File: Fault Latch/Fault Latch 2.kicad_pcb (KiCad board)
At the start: 2 copper layers, 85 x 85 mm, 116 parts, among them J1 1053141312, J3 1053131202, J4 1053131202, J5 1053131202, K3 Fujitsu_FTR-LYCA005x, K5 Fujitsu_FTR-LYCA005x, K6 Fujitsu_FTR-LYCA005x, Q101 Q_NPN_BEC, Q102 Q_NPN_BEC, Q103 Q_NPN_BEC, Q104 Q_NPN_BEC, Q105 Q_NMOS_GSD, Q106 Q_NMOS_GSD, Q110 Q_NPN_BEC, Q111 Q_NPN_BEC, Q112 Q_NMOS_GSD, Q113 Q_NMOS_GSD, Q114 Q_NMOS_GSD, Q115 Q_NMOS_GSD, Q117 Q_NMOS_GSD, Q118 Q_NMOS_GSD, Q119 Q_NMOS_GSD, Q120 Q_NMOS_GSD, Q121 Q_NMOS_GSD, Q122 Q_NMOS_GSD, Q123 Q_NMOS_GSD, Q124 Q_NMOS_GSD, Q125 Q_NMOS_GSD, SW101 SW_Omron_B3FS, SW102 SW_Omron_B3FS, SW103 SW_Omron_B3FS, U1 74LS279, U104 74AHC1G00, U109 74AHC1G00, U112 74AHC1G00, U117 74AHC1G00, U118 LM555xM, U2 LM1117DT-5.0, U7 SN74AHC1G08DBVR, U8 SN74AHC1G08DBVR

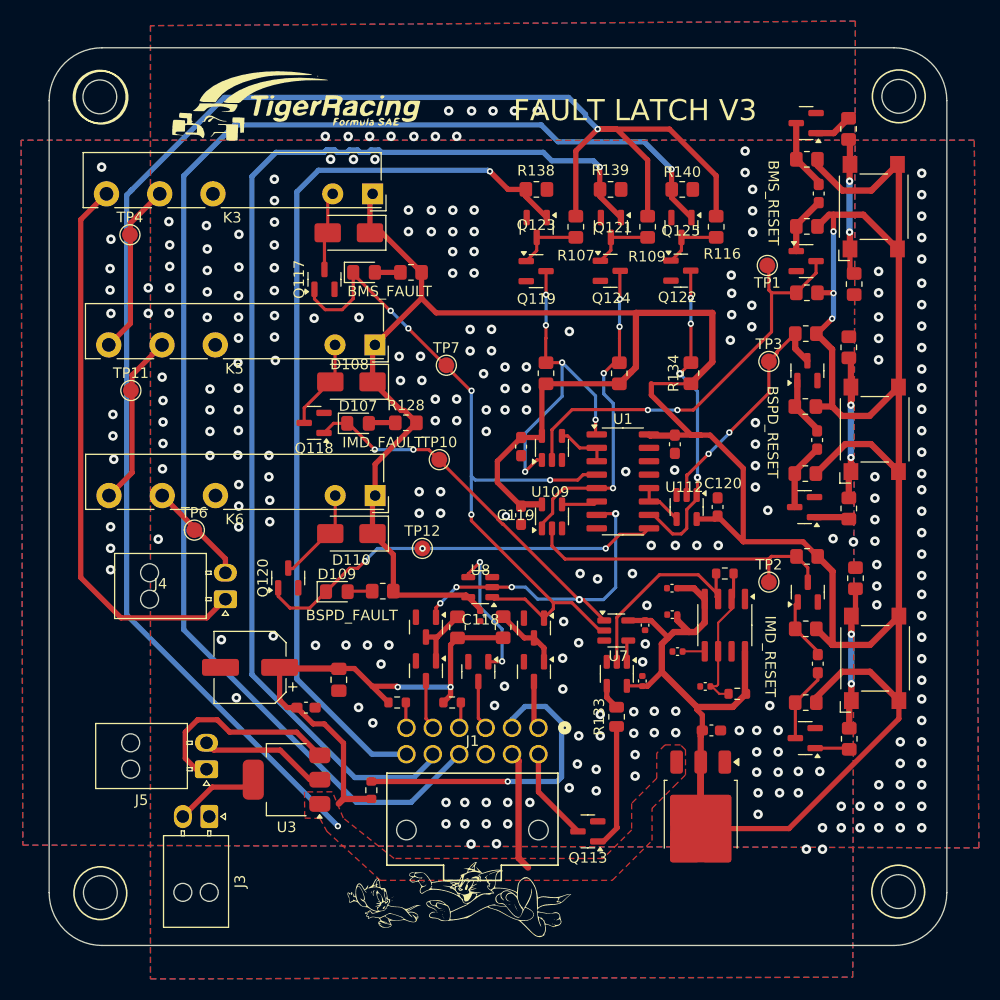
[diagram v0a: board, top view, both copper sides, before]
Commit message: Fault Latch reivision
Currently fixing the 2026 iteration of the fault latch.
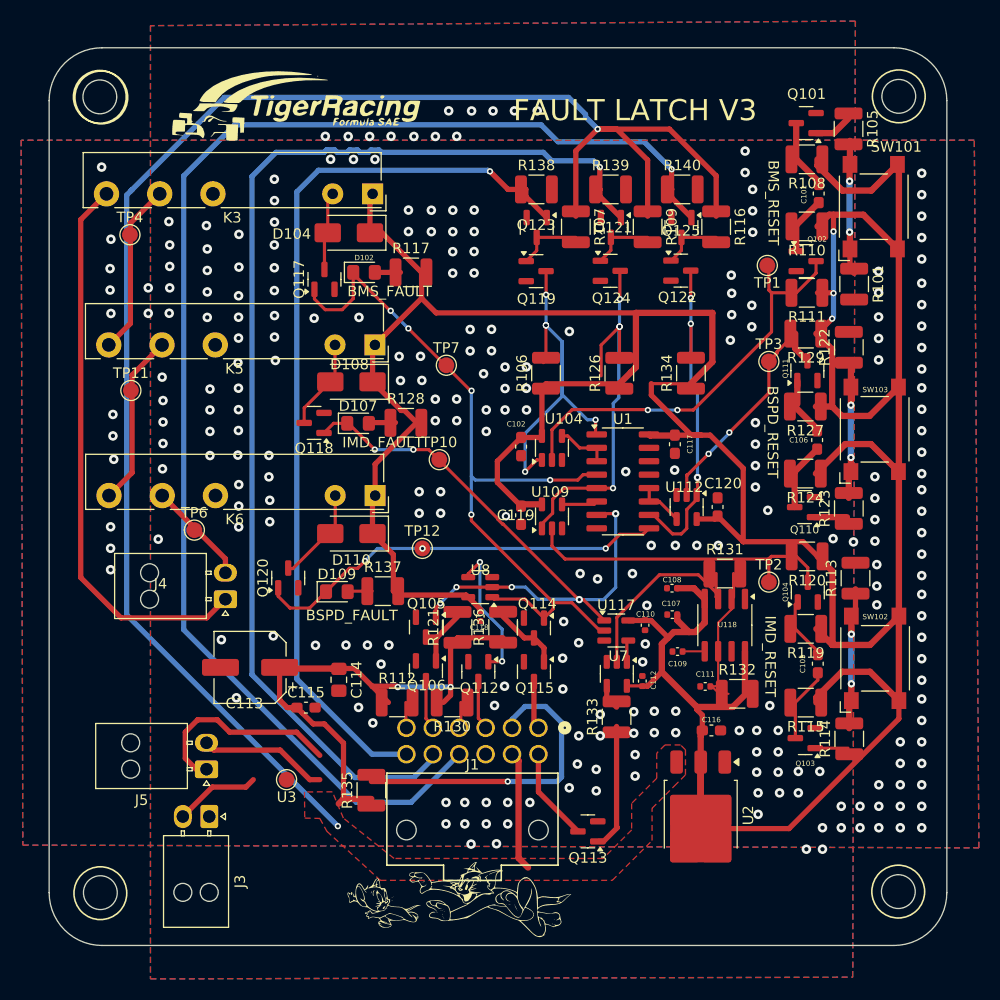
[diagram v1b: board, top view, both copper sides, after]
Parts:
- R101, R105, R106, R107, R108, R109, R110, R111, R113, R114, R115, R116, R117, R119, R120, R121, R122, R123, R124, R126, R127, R128, R129, R134, R136, R137, R138, R139, R140: footprint Resistor_SMD:R_0805_2012Metric_Pad1.20x1.40mm_HandSolder -> Resistor_SMD:R_1210_3225Metric
- R112, R130, R131, R132, R135: footprint Resistor_SMD:R_0603_1608Metric -> Resistor_SMD:R_1210_3225Metric
- R133: footprint Resistor_SMD:R_0805_2012Metric -> Resistor_SMD:R_1210_3225Metric
- TP1: value TestPoint_BMS -> TestPoint
- TP10, TP12, TP7: value TestPoint_SR_BMS -> TestPoint
- TP11: value TestPoint_IMD_Shutdown -> TestPoint
- TP2: value TestPoint_IMD -> TestPoint
- TP3: value TestPoint_BSPD -> TestPoint
- TP4: value TestPoint_BMS_Shutdown -> TestPoint
- TP6: value TestPoint_BSPD_Shutdown -> TestPoint
- U3: value ~ -> TestPoint; footprint Package_TO_SOT_SMD:SOT-223 -> TestPoint:TestPoint_Pad_D1.5mm
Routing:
- net /NIMD_LV: track 30.3 -> 38.5 mm
- net /NBMS_LV: track 32.3 -> 37.2 mm
- net /NBPSD_LV: track 29.5 -> 32.4 mm, vias 4 -> 3
- net Net-(Q113-G): vias 0 -> 2
- net GND: vias 260 -> 258
